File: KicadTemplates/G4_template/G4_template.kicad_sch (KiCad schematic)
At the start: 10 parts, among them J1 Conn_01x04_Female, J2 Conn_01x03_Male, J3 Conn_01x03_Male, J4 Conn_02x10_Odd_Even, J5 Conn_02x03_Odd_Even, J6 Conn_01x01_Female, SW1 SW_SPDT, U2 NUCLEO-G491RE

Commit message: updated template
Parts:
- removed U2: NUCLEO-G491RE, G4Lib:MODULE_NUCLEO-G491RE20, symbol nucleo64:NUCLEO-G491RE
- added J_PWR1: Conn_01x05_Female, Connector_JST:JST_XH_S5B-XH-A_1x05_P2.50mm_Horizontal, symbol Connector:Conn_01x05_Female
- added R1, R2: 4.4K, Resistor_THT:R_Axial_DIN0207_L6.3mm_D2.5mm_P7.62mm_Horizontal, symbol Device:R
- added U1: NUCLEO-G491RE, G4Lib:MODULE_NUCLEO-G491RE20, symbol nucleo64:NUCLEO-G491RE_SER
- renumbered J6 to J_GND1, J5 to J_POW1, J2 to J_SRV1, J3 to J_SRV2, J4 to J_TRACK1
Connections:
- net 12V: now also J_PWR1.1 (Pin_1)
- net 3V3: now also J1.3 (Pin_3), R1.2, R2.2
- net 5V: now also J_PWR1.3 (Pin_3)
- net GND: now also J1.4 (Pin_4), J_PWR1.2 (Pin_2), U1.CN7_19 (CN7_GND), U1.CN7_20 (CN7_GND), U1.CN7_22 (CN7_GND), U1.CN7_8 (CN7_GND)
- net I2C3_DTA: now reaches J1.1 (Pin_1)
- net I2C3_DTA: now also R1.1
- net I2C3_CK: now reaches J1.2 (Pin_2)
- net I2C3_CK: now also R2.1
- net CANH: now reaches J_BUS1.4 (Pin_4), J_BUS2.4 (Pin_4)
- net CANL: now reaches J_BUS1.5 (Pin_5), J_BUS2.5 (Pin_5)
- new net: U1.CN10_3 (PB8/CAN1RX), U1.SER0
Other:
- note added: "SSD1306 DISPLAY"
- moved on the sheet: J_GND1, J_SRV2

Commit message: update spec
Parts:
- added R3, R4: 4.4K, Resistor_THT:R_Axial_DIN0207_L6.3mm_D2.5mm_P7.62mm_Horizontal, symbol Device:R
- added R5: 20K, Resistor_THT:R_Axial_DIN0207_L6.3mm_D2.5mm_P7.62mm_Horizontal, symbol Device:R
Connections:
- net I2C3_CK is gone; now on net I2C3_SCL: J1.2 (Pin_2), R2.1
- net 3V3: now also U1.CN7_5 (VDD), R3.2, R4.2
- net 5VCPU: now also U1.CN7_18 (CN7_+5V); no longer SW1.3 (C)
- net GND: now also U1.CN10_20 (CN10_GND), U1.CN10_9 (CN10_GND), R5.1
- net R0A: no longer J_TRACK1.15 (Pin_15)
- net R0B: no longer J_TRACK1.16 (Pin_16)
- net R1A: no longer J_TRACK1.17 (Pin_17)
- net R1B: no longer J_TRACK1.18 (Pin_18)
- net R2A: no longer J_TRACK1.19 (Pin_19)
- net R2B: no longer J_TRACK1.20 (Pin_20)
- net at U1.SER0: no longer U1.CN10_3 (PB8/CAN1RX)
- net S_IN: now reaches U1.SER3
- net S_IN: now also U1.CN10_5 (PB9)
- net I2C3_SDA: now reaches U1.CN10_1 (PC9)
- net LD2: now reaches U1.CN10_11 (PA5)
- net CAN_TX: now reaches U1.CN10_12 (PA12)
- net ADC2_IN3: now reaches U1.CN10_13 (PA6)
- net CAN_RX: now reaches U1.CN10_14 (PA11)
- net ADC2_IN4: now reaches U1.CN10_15 (PA7)
- net I2C3_SCL: now reaches U1.CN10_2 (PC8)
- net PWM_0_1: now reaches U1.CN10_21 (PA9)
- net EECS: now reaches U1.CN10_22 (PB2)
- net PWM_0_0: now reaches U1.CN10_23 (PA8)
- net PWM_3_1: now reaches U1.CN10_24 (PB1)
- net TIM2_CH3: now reaches U1.CN10_25 (PB10)
- net SPI2_MOSI: now reaches U1.CN10_26 (PB15)
- net SPI2_MISO: now reaches U1.CN10_28 (PB14)
- net SPI2_SCK: now reaches U1.CN10_30 (PB13)
- net SWO: now reaches U1.CN10_31 (PB3)
- net PWM_1_0: now reaches U1.CN10_33 (PA10)
- net ADC2_IN5: now reaches U1.CN10_34 (PC4)
- net PWM_2_0: now reaches U1.CN10_4 (PC6)
- net ASENSE: now reaches U1.CN10_6 (PC5)
- net ASENSE: now also R5.2
- net SPI3_SCK: now reaches U1.CN7_1 (PC10/SPI3_SCK)
- net SWDIO: now reaches U1.CN7_13 (PA13)
- net SWDCLK: now reaches U1.CN7_15 (PA14)
- net I2C1_SCL: now reaches U1.CN7_17 (PA15)
- net I2C1_SCL: now also R4.1
- net S_VALID: now reaches U1.CN7_2 (PC11/SPI3_MISO)
- net I2C1_SDA: now reaches U1.CN7_21 (PB7)
- net ADC2_IN1: now reaches U1.CN7_28 (PA0)
- net SPI3_MOSI: now reaches U1.CN7_3 (PC12/SPI3_MOSI)
- net ADC2_IN2: now reaches U1.CN7_30 (PA1)
- net PWM_2_1: now reaches U1.CN7_32 (PA4)
- net PWM_3_0: now reaches U1.CN7_34 (PB0)
- net ADC2_IN8: now reaches U1.CN7_35 (PC2)
- net ADC2_IN7: now reaches U1.CN7_36 (PC1/PB9)
- net PWM_1_1: now reaches U1.CN7_37 (PC3)
- net ADC2_IN6: now reaches U1.CN7_38 (PC0/PB8)
- net S_CLR: now reaches U1.CN7_4 (PD2)
- net 5VCPU_IN: now reaches U1.CN7_6 (E5V)
- net 5VCPU_IN: now also SW1.3 (C)
- new net I2C1_DTA: R3.1
- new net TIM2_CH4: U1.CN10_18 (PB11)
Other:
- note added: "for CAN module"
- note added: "ina3221 i2c"
- company: (none) -> DBN
- title: (none) -> Template G4 V2
- moved on the sheet: J_POW1, J_PWR1, J_TRACK1, SW1, U1G

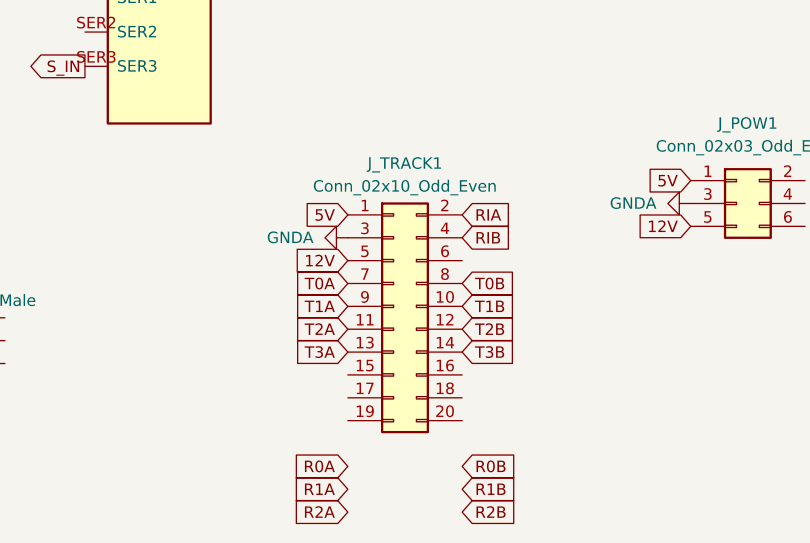
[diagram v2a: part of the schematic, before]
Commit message: update spec J_TRACK and mapping
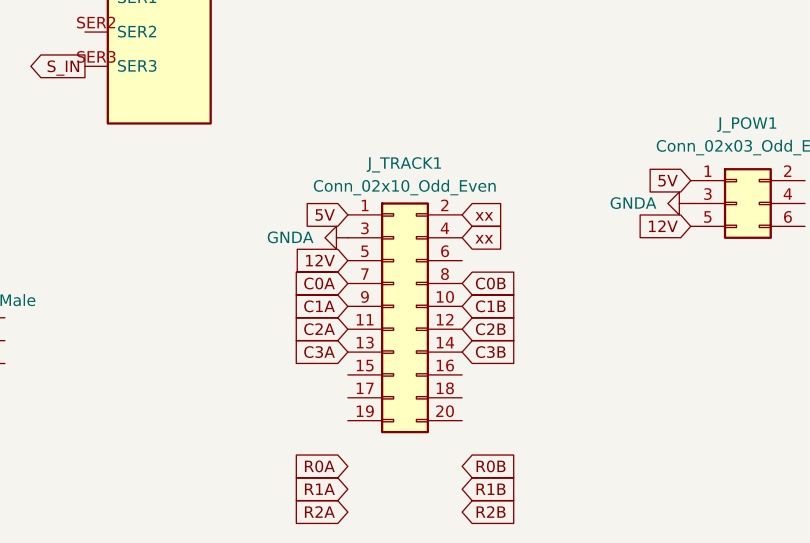
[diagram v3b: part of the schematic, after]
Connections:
- net RIB is gone; now on net xx: J_TRACK1.4 (Pin_4)
- net RIA renamed xx
- net T0A renamed C0A
- net T0B renamed C0B
- net T1A renamed C1A
- net T1B renamed C1B
- net T2A renamed C2A
- net T2B renamed C2B
- net T3A renamed C3A
- net T3B renamed C3B
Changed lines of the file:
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@@
     )
   )
-  (global_label "RIB" (shape input) (at 134.62 157.48 0) (fields_autoplaced)
-    (effects (font (size 1.27 1.27)) (justify left))
-    (property "Intersheetrefs" "${INTERSHEET_REFS}" (at 140.1779 157.5594 0)
-      (effects (font (size 1.27 1.27)) (justify left) hide)
-    )
-  )
-  (global_label "T1B" (shape input) (at 134.62 165.1 0) (fields_autoplaced)
-    (effects (font (size 1.27 1.27)) (justify left))
-    (property "Intersheetrefs" "${INTERSHEET_REFS}" (at 140.4802 165.0206 0)
+  (global_label "xx" (shape input) (at 134.62 157.48 0) (fields_autoplaced)
+    (effects (font (size 1.27 1.27)) (justify left))
+    (property "Intersheetrefs" "${INTERSHEET_REFS}" (at 139.6614 157.48 0)
+      (effects (font (size 1.27 1.27)) (justify left) hide)
+    )
+  )
+  (global_label "C1B" (shape input) (at 134.62 165.1 0) (fields_autoplaced)
+    (effects (font (size 1.27 1.27)) (justify left))
+    (property "Intersheetrefs" "${INTERSHEET_REFS}" (at 141.3547 165.1 0)
       (effects (font (size 1.27 1.27)) (justify left) hide)
     )
@@
     )
   )
-  (global_label "T0B" (shape input) (at 134.62 162.56 0) (fields_autoplaced)
-    (effects (font (size 1.27 1.27)) (justify left))
-    (property "Intersheetrefs" "${INTERSHEET_REFS}" (at 140.4802 162.4806 0)
-      (effects (font (size 1.27 1.27)) (justify left) hide)
-    )
-  )
-  (global_label "RIA" (shape input) (at 134.62 154.94 0) (fields_autoplaced)
-    (effects (font (size 1.27 1.27)) (justify left))
-    (property "Intersheetrefs" "${INTERSHEET_REFS}" (at 139.9964 154.8606 0)
+  (global_label "C0B" (shape input) (at 134.62 162.56 0) (fields_autoplaced)
+    (effects (font (size 1.27 1.27)) (justify left))
+    (property "Intersheetrefs" "${INTERSHEET_REFS}" (at 141.3547 162.56 0)
+      (effects (font (size 1.27 1.27)) (justify left) hide)
+    )
+  )
+  (global_label "xx" (shape input) (at 134.62 154.94 0) (fields_autoplaced)
+    (effects (font (size 1.27 1.27)) (justify left))
+    (property "Intersheetrefs" "${INTERSHEET_REFS}" (at 139.6614 154.94 0)
       (effects (font (size 1.27 1.27)) (justify left) hide)
     )
@@
     )
   )
-  (global_label "T3A" (shape input) (at 121.92 170.18 180) (fields_autoplaced)
-    (effects (font (size 1.27 1.27)) (justify right))
-    (property "Intersheetrefs" "${INTERSHEET_REFS}" (at 116.2412 170.1006 0)
+  (global_label "C3A" (shape input) (at 121.92 170.18 180) (fields_autoplaced)
+    (effects (font (size 1.27 1.27)) (justify right))
+    (property "Intersheetrefs" "${INTERSHEET_REFS}" (at 115.3667 170.18 0)
       (effects (font (size 1.27 1.27)) (justify right) hide)
     )
@@
     )
   )
-  (global_label "T0A" (shape input) (at 121.92 162.56 180) (fields_autoplaced)
-    (effects (font (size 1.27 1.27)) (justify right))
-    (property "Intersheetrefs" "${INTERSHEET_REFS}" (at 116.2412 162.4806 0)
+  (global_label "C0A" (shape input) (at 121.92 162.56 180) (fields_autoplaced)
+    (effects (font (size 1.27 1.27)) (justify right))
+    (property "Intersheetrefs" "${INTERSHEET_REFS}" (at 115.3667 162.56 0)
       (effects (font (size 1.27 1.27)) (justify right) hide)
     )
@@
     )
   )
-  (global_label "T3B" (shape input) (at 134.62 170.18 0) (fields_autoplaced)
-    (effects (font (size 1.27 1.27)) (justify left))
-    (property "Intersheetrefs" "${INTERSHEET_REFS}" (at 140.4802 170.1006 0)
+  (global_label "C3B" (shape input) (at 134.62 170.18 0) (fields_autoplaced)
+    (effects (font (size 1.27 1.27)) (justify left))
+    (property "Intersheetrefs" "${INTERSHEET_REFS}" (at 141.3547 170.18 0)
       (effects (font (size 1.27 1.27)) (justify left) hide)
     )
@@
     )
   )
-  (global_label "T2B" (shape input) (at 134.62 167.64 0) (fields_autoplaced)
-    (effects (font (size 1.27 1.27)) (justify left))
-    (property "Intersheetrefs" "${INTERSHEET_REFS}" (at 140.4802 167.5606 0)
+  (global_label "C2B" (shape input) (at 134.62 167.64 0) (fields_autoplaced)
+    (effects (font (size 1.27 1.27)) (justify left))
+    (property "Intersheetrefs" "${INTERSHEET_REFS}" (at 141.3547 167.64 0)
       (effects (font (size 1.27 1.27)) (justify left) hide)
     )
@@
     )
   )
-  (global_label "T2A" (shape input) (at 121.92 167.64 180) (fields_autoplaced)
-    (effects (font (size 1.27 1.27)) (justify right))
-    (property "Intersheetrefs" "${INTERSHEET_REFS}" (at 116.2412 167.5606 0)
+  (global_label "C2A" (shape input) (at 121.92 167.64 180) (fields_autoplaced)
+    (effects (font (size 1.27 1.27)) (justify right))
+    (property "Intersheetrefs" "${INTERSHEET_REFS}" (at 115.3667 167.64 0)
       (effects (font (size 1.27 1.27)) (justify right) hide)
     )
@@
     )
   )
-  (global_label "T1A" (shape input) (at 121.92 165.1 180) (fields_autoplaced)
-    (effects (font (size 1.27 1.27)) (justify right))
-    (property "Intersheetrefs" "${INTERSHEET_REFS}" (at 116.2412 165.0206 0)
-      (effects (font (size 1.27 1.27)) (justify right) hide)
-    )
+  (global_label "C1A" (shape input) (at 121.92 165.1 180) (fields_autoplaced)
+    (effects (font (size 1.27 1.27)) (justify right))
+    (property "Intersheetrefs" "${INTERSHEET_REFS}" (at 115.3667 165.1 0)
+      (effects (font (size 1.27 1.27)) (justify right) hide)
+    )

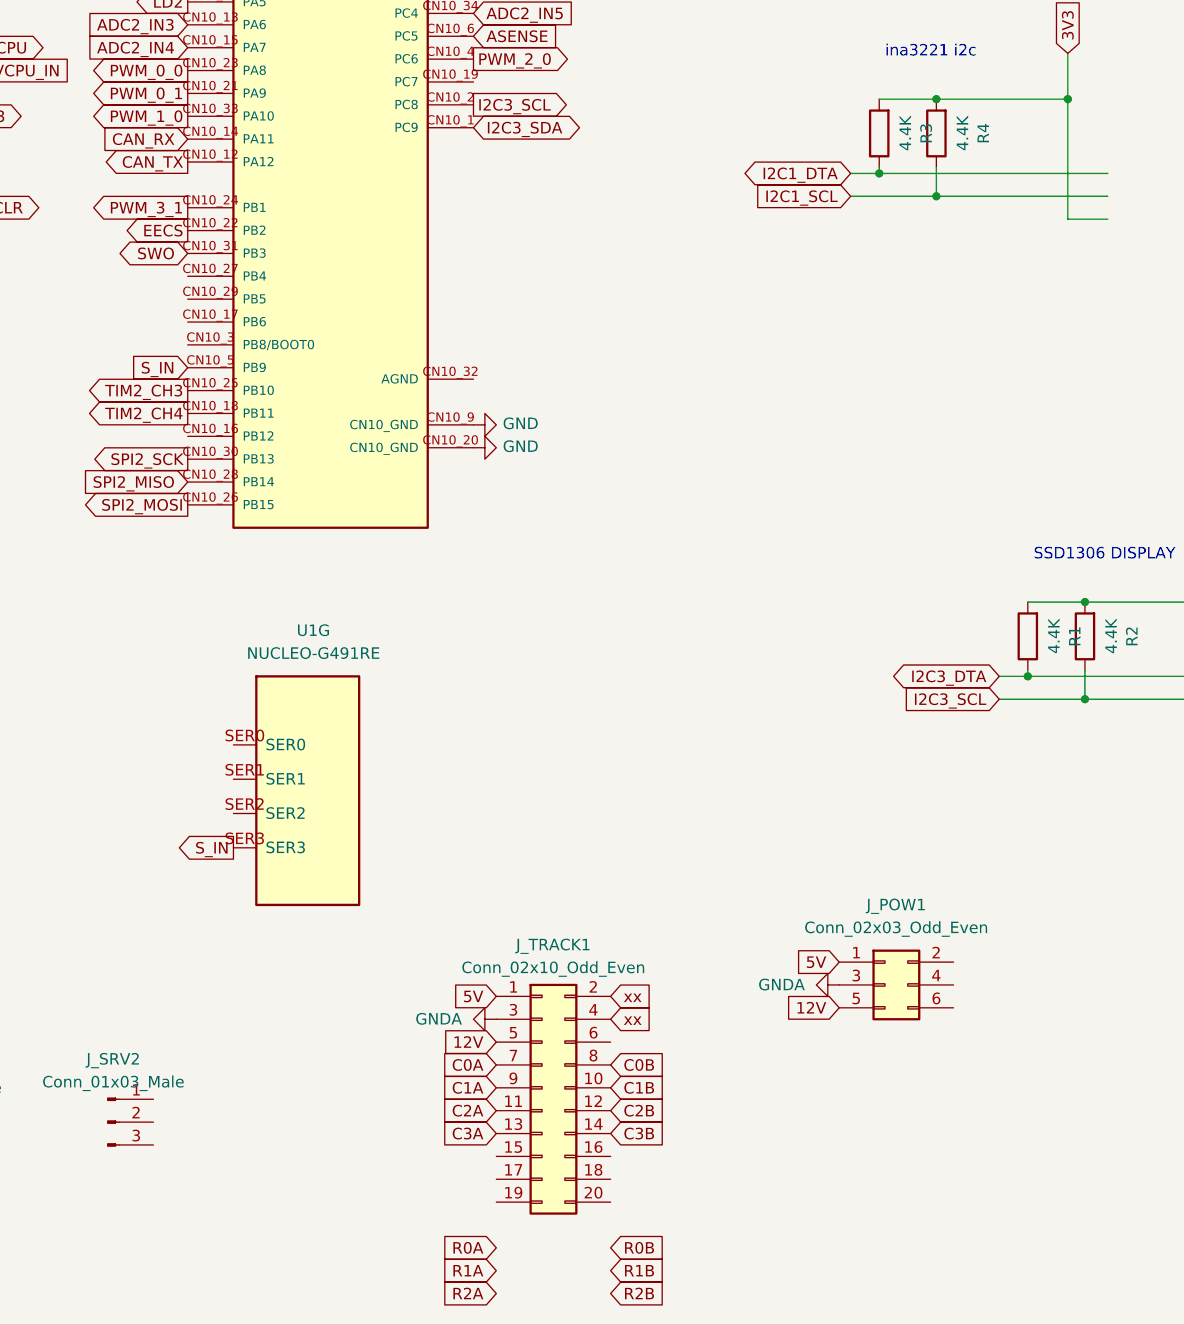
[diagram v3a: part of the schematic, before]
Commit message: update spec J_TRACK and mapping
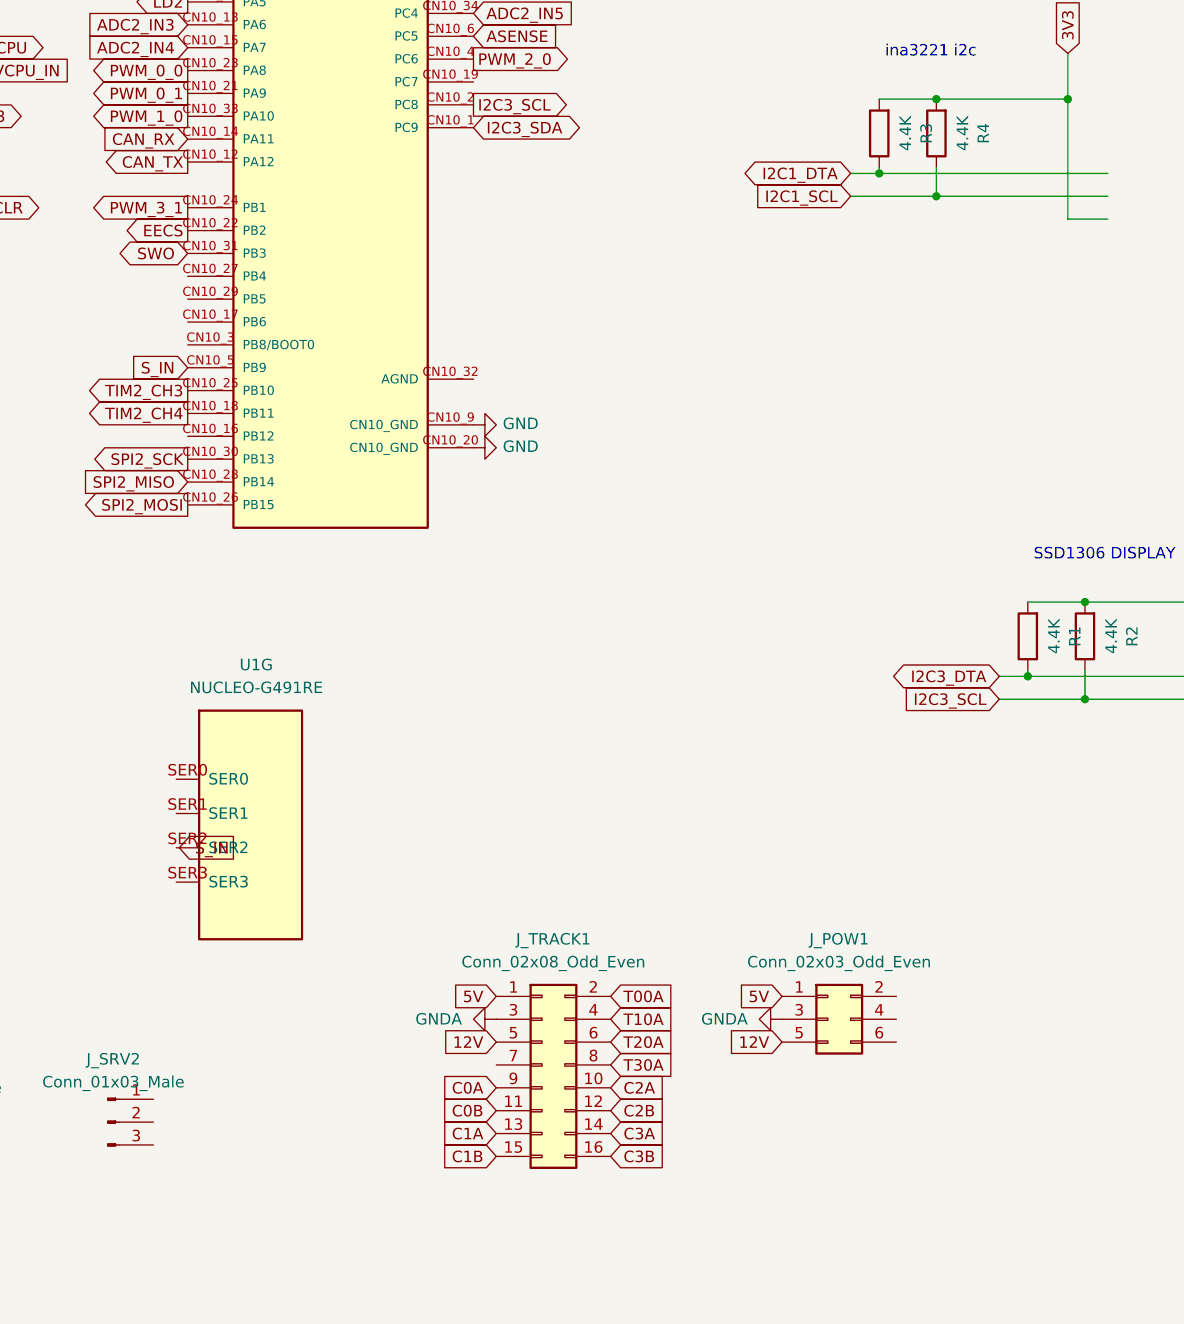
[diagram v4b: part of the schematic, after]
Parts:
- removed J_TRACK1: Conn_02x10_Odd_Even, Connector_PinHeader_2.54mm:PinHeader_2x10_P2.54mm_Vertical, symbol Connector_Generic:Conn_02x10_Odd_Even
- added J_TRACK1: Conn_02x08_Odd_Even, Connector_PinHeader_2.54mm:PinHeader_2x08_P2.54mm_Vertical, symbol Connector_Generic:Conn_02x08_Odd_Even
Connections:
- net 12V: now also J_TRACK1.5 (Pin_5)
- net 5V: now also J_TRACK1.1 (Pin_1)
- net C0A: now also J_TRACK1.9 (Pin_9)
- net C0B: now also J_TRACK1.11 (Pin_11)
- net C1A: now also J_TRACK1.13 (Pin_13)
- net C1B: now also J_TRACK1.15 (Pin_15)
- net C2A: now also J_TRACK1.10 (Pin_10)
- net C2B: now also J_TRACK1.12 (Pin_12)
- net C3A: now also J_TRACK1.14 (Pin_14)
- net C3B: now also J_TRACK1.16 (Pin_16)
- net GND: now also J_TRACK1.3 (Pin_3)
- net S_IN: no longer U1.SER3
- new net T00A: J_TRACK1.2 (Pin_2)
- new net T10A: J_TRACK1.4 (Pin_4)
- new net T20A: J_TRACK1.6 (Pin_6)
- new net T30A: J_TRACK1.8 (Pin_8)
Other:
- moved on the sheet: J_POW1, U1G

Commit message: update spec POW_CTRL
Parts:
- added JP1, JP2, JP3, JP4, JP5, JP6, JP7, JP8, JP9: SolderJumper_2_Open, Jumper:SolderJumper-2_P1.3mm_Open_Pad1.0x1.5mm, symbol Jumper:SolderJumper_2_Open
- added R_IDENT1: ~, Resistor_THT:R_Axial_DIN0207_L6.3mm_D2.5mm_P7.62mm_Horizontal, symbol Device:R
- added U3: 74HC594, Package_DIP:DIP-16_W7.62mm_LongPads, symbol DBN:74HC594
- J_PWR1: footprint Connector_JST:JST_XH_S5B-XH-A_1x05_P2.50mm_Horizontal -> Connector_JST:JST_XH_S4B-XH-A-1_1x04_P2.50mm_Horizontal; symbol Connector:Conn_01x05_Female -> Connector:Conn_01x04_Socket
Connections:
- net ASENSE: now also R_IDENT1.1
- net SPI3_MOSI: now also JP1.1 (A)
- net S_CLR: now also U3.10 (~{SRCLR}), U3.13 (~{RCLR})
- net S_VALID: now also U3.12 (RCLK)
- net POW_CTRL: now reaches J_PWR1.4 (Pin_4)
- net POW_CTRL: now also U1.CN10_27 (PB4)
- net S_IN renamed SER3
- net SER3: now also JP5.1 (A), JP9.2 (B)
- new net: JP6.1 (A), JP7.1 (A), JP8.1 (A), JP9.1 (A), R_IDENT1.2, U3.9 (QH')
- new net: JP1.2 (B), JP2.2 (B), JP3.2 (B), JP4.2 (B), JP5.2 (B), U3.14 (SER)
- new net SER0: JP2.1 (A), JP6.2 (B)
- new net SER1: JP3.1 (A), JP7.2 (B)
- new net SER2: JP4.1 (A), JP8.2 (B)
- new net SPI3_CLK: U3.11 (SRCLK)
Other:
- moved on the sheet: J1, J_BUS1, J_BUS2, J_GND1, J_POW1, J_TRACK1, R1, R2, SW1

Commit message: updated template
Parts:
- removed JP1, JP2, JP3, JP4, JP5, JP6, JP7, JP8, JP9: SolderJumper_2_Open, Jumper:SolderJumper-2_P1.3mm_Open_Pad1.0x1.5mm, symbol Jumper:SolderJumper_2_Open
- added JP1, JP2, JP3, JP4, JP5, JP6, JP7, JP8, JP9: Jumper_2_Open, Connector_PinHeader_2.54mm:PinHeader_1x02_P2.54mm_Vertical, symbol Jumper:Jumper_2_Open
- added J_AGND1: Conn_01x01_Female, Connector_PinHeader_2.54mm:PinHeader_1x01_P2.54mm_Vertical, symbol Connector:Conn_01x01_Female
- renumbered R_IDENT1 to R_ID1
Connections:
- net SPI3_CLK is gone; now on net SPI3_SCK: U3.11 (SRCLK)
- net GND: now also J_AGND1.1 (Pin_1)
- net SER0: now also JP6.2 (B)
- net SER1: now also JP7.2 (B)
- net SER2: now also JP8.2 (B)
- net SER3: now also JP9.2 (B)
- net at R_ID1.2, U3.9 (QH'): now also JP6.1 (A), JP7.1 (A), JP8.1 (A), JP9.1 (A)
- net at U3.14 (SER): now also JP1.2 (B), JP2.2 (B), JP3.2 (B), JP4.2 (B), JP5.2 (B)
